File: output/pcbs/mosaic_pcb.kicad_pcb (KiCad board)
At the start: 2 copper layers, 100 x 95 mm, 20 parts

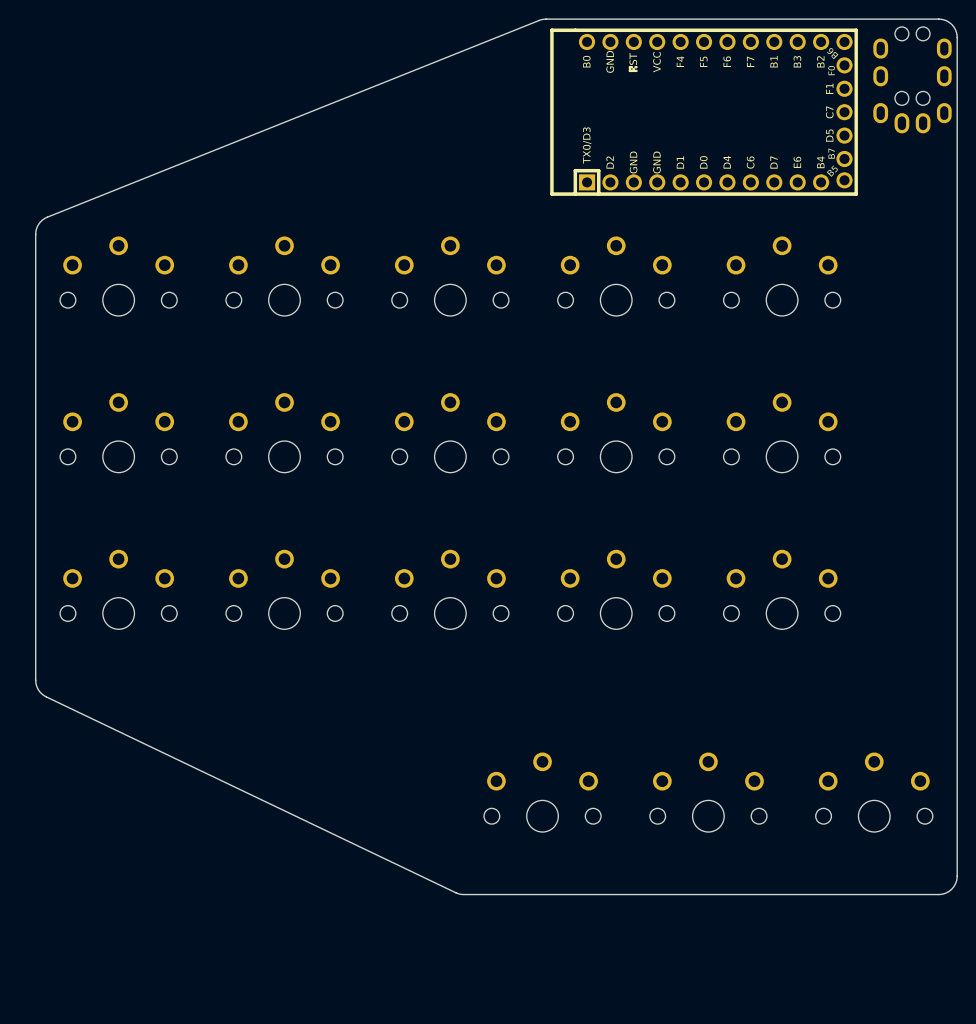
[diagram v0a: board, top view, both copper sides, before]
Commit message: xiao-based, sub 100mm^2
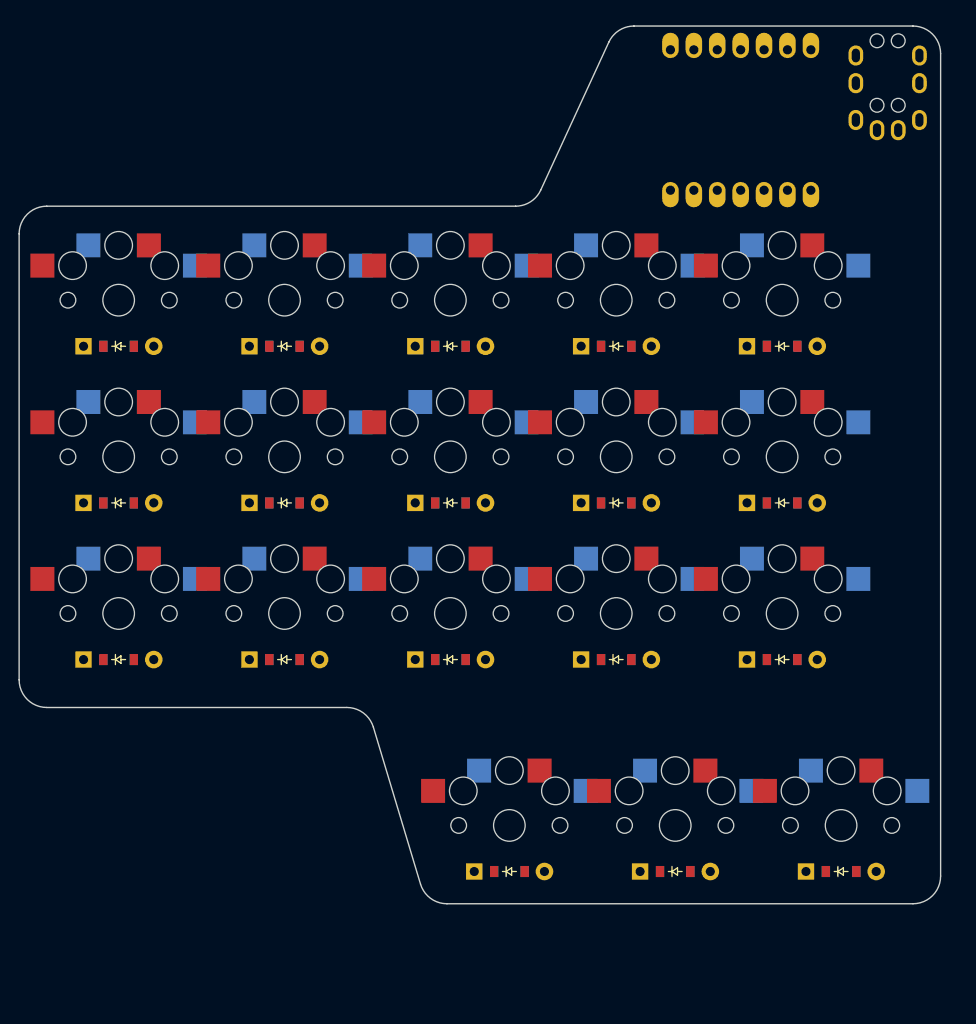
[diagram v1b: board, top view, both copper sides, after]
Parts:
- removed the ? at (208.8, 81.6)
- added ?: , xiao-tht, F.Cu at (211.5, 82.5)
- added D1: , ComboDiode, F.Cu at (144.0, 141.0)
- added D10: , ComboDiode, F.Cu at (198.0, 141.0)
- added D11: , ComboDiode, F.Cu at (198.0, 124.0)
- added D12: , ComboDiode, F.Cu at (198.0, 107.0)
- added D13: , ComboDiode, F.Cu at (216.0, 141.0)
- added D14: , ComboDiode, F.Cu at (216.0, 124.0)
- added D15: , ComboDiode, F.Cu at (216.0, 107.0)
- added D16: , ComboDiode, F.Cu at (186.4, 164.0)
- added D17: , ComboDiode, F.Cu at (204.4, 164.0)
- added D18: , ComboDiode, F.Cu at (222.4, 164.0)
- added D2: , ComboDiode, F.Cu at (144.0, 124.0)
- added D3: , ComboDiode, F.Cu at (144.0, 107.0)
- added D4: , ComboDiode, F.Cu at (162.0, 141.0)
- added D5: , ComboDiode, F.Cu at (162.0, 124.0)
- added D6: , ComboDiode, F.Cu at (162.0, 107.0)
- added D7: , ComboDiode, F.Cu at (180.0, 141.0)
- added D8: , ComboDiode, F.Cu at (180.0, 124.0)
- added D9: , ComboDiode, F.Cu at (180.0, 107.0)
- moved S16 3.74 mm to (186.4, 159.0)
- moved S17 3.74 mm to (204.4, 159.0)
- moved S18 3.74 mm to (222.4, 159.0)
- moved TRRS1 2.80 mm to (228.6, 72.2)
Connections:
- S1 pad 1: matrix_pinky_bottom -> D0
- S1 pad 2: GND -> pinky_bottom
- S10 pad 1: matrix_index_bottom -> D3
- S10 pad 2: GND -> index_bottom
- S11 pad 1: matrix_index_home -> D3
- S11 pad 2: GND -> index_home
- S12 pad 1: matrix_index_top -> D3
- S12 pad 2: GND -> index_top
- S13 pad 1: matrix_inner_bottom -> D4
- S13 pad 2: GND -> inner_bottom
- S14 pad 1: matrix_inner_home -> D4
- S14 pad 2: GND -> inner_home
- S15 pad 1: matrix_inner_top -> D4
- S15 pad 2: GND -> inner_top
- S16 pad 1: thumbfan_near_home -> D2
- S16 pad 2: GND -> near_home
- S17 pad 1: thumbfan_home_home -> D3
- S17 pad 2: GND -> home_home
- S18 pad 1: thumbfan_far_home -> D4
- S18 pad 2: GND -> far_home
- S2 pad 1: matrix_pinky_home -> D0
- S2 pad 2: GND -> pinky_home
- S3 pad 1: matrix_pinky_top -> D0
- S3 pad 2: GND -> pinky_top
- S4 pad 1: matrix_ring_bottom -> D1
- S4 pad 2: GND -> ring_bottom
- S5 pad 1: matrix_ring_home -> D1
- S5 pad 2: GND -> ring_home
- S6 pad 1: matrix_ring_top -> D1
- S6 pad 2: GND -> ring_top
- S7 pad 1: matrix_middle_bottom -> D2
- S7 pad 2: GND -> middle_bottom
- S8 pad 1: matrix_middle_home -> D2
- S8 pad 2: GND -> middle_home
- S9 pad 1: matrix_middle_top -> D2
- S9 pad 2: GND -> middle_top
- TRRS1 pad 2: VCC -> SV
- TRRS1 pad 3: D3 -> D7
- TRRS1 pad 4: D2 -> D6
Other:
- board size 100 x 95 mm -> 100 x 95.2 mm

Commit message: rp2040 zero,diodeless, hotswap
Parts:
- removed the ? at (211.5, 82.5)
- removed D1, D10, D11, D12, D13, D14, D15, D16, D17, D18, D2, D3, D4, D5, D6, D7, D8, D9: , ComboDiode
- added ?: , rp2040_zero_tht_pads, F.Cu at (145.8, 154.7)
- added REF**: VIA-0.6mm, VIA-0.6mm, F.Cu at (144.0, 133.0)
- added REF**: VIA-0.6mm, VIA-0.6mm, F.Cu at (198.0, 133.0)
- added REF**: VIA-0.6mm, VIA-0.6mm, F.Cu at (198.0, 116.0)
- added REF**: VIA-0.6mm, VIA-0.6mm, F.Cu at (198.0, 99.0)
- added REF**: VIA-0.6mm, VIA-0.6mm, F.Cu at (216.0, 133.0)
- added REF**: VIA-0.6mm, VIA-0.6mm, F.Cu at (216.0, 116.0)
- added REF**: VIA-0.6mm, VIA-0.6mm, F.Cu at (216.0, 99.0)
- added REF**: VIA-0.6mm, VIA-0.6mm, F.Cu at (186.4, 160.2)
- added REF**: VIA-0.6mm, VIA-0.6mm, F.Cu at (204.4, 160.2)
- added REF**: VIA-0.6mm, VIA-0.6mm, F.Cu at (222.4, 160.2)
- added REF**: VIA-0.6mm, VIA-0.6mm, F.Cu at (144.0, 116.0)
- added REF**: VIA-0.6mm, VIA-0.6mm, F.Cu at (144.0, 99.0)
- added REF**: VIA-0.6mm, VIA-0.6mm, F.Cu at (162.0, 133.0)
- added REF**: VIA-0.6mm, VIA-0.6mm, F.Cu at (162.0, 116.0)
- added REF**: VIA-0.6mm, VIA-0.6mm, F.Cu at (162.0, 99.0)
- added REF**: VIA-0.6mm, VIA-0.6mm, F.Cu at (180.0, 133.0)
- added REF**: VIA-0.6mm, VIA-0.6mm, F.Cu at (180.0, 116.0)
- added REF**: VIA-0.6mm, VIA-0.6mm, F.Cu at (180.0, 99.0)
- moved TRRS1 78.3 mm to (233.1, 150.4), turned to 270 degrees
- moved S16 4.20 mm to (186.4, 163.2)
- moved S17 4.20 mm to (204.4, 163.2)
- moved S18 4.20 mm to (222.4, 163.2)
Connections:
- S1 pad 1: D0 -> matrix_pinky_bottom
- S1 pad 2: pinky_bottom -> GND
- S10 pad 1: D3 -> matrix_index_bottom
- S10 pad 2: index_bottom -> GND
- S11 pad 1: D3 -> matrix_index_home
- S11 pad 2: index_home -> GND
- S12 pad 1: D3 -> matrix_index_top
- S12 pad 2: index_top -> GND
- S13 pad 1: D4 -> matrix_inner_bottom
- S13 pad 2: inner_bottom -> GND
- S14 pad 1: D4 -> matrix_inner_home
- S14 pad 2: inner_home -> GND
- S15 pad 1: D4 -> matrix_inner_top
- S15 pad 2: inner_top -> GND
- S16 pad 1: D2 -> thumbfan_near_home
- S16 pad 2: near_home -> GND
- S17 pad 1: D3 -> thumbfan_home_home
- S17 pad 2: home_home -> GND
- S18 pad 1: D4 -> thumbfan_far_home
- S18 pad 2: far_home -> GND
- S2 pad 1: D0 -> matrix_pinky_home
- S2 pad 2: pinky_home -> GND
- S3 pad 1: D0 -> matrix_pinky_top
- S3 pad 2: pinky_top -> GND
- S4 pad 1: D1 -> matrix_ring_bottom
- S4 pad 2: ring_bottom -> GND
- S5 pad 1: D1 -> matrix_ring_home
- S5 pad 2: ring_home -> GND
- S6 pad 1: D1 -> matrix_ring_top
- S6 pad 2: ring_top -> GND
- S7 pad 1: D2 -> matrix_middle_bottom
- S7 pad 2: middle_bottom -> GND
- S8 pad 1: D2 -> matrix_middle_home
- S8 pad 2: middle_home -> GND
- S9 pad 1: D2 -> matrix_middle_top
- S9 pad 2: middle_top -> GND
- TRRS1 pad 1: GND -> 3V3
- TRRS1 pad 2: SV -> GND
- TRRS1 pad 3: D7 -> GP9
- TRRS1 pad 4: D6 -> GP8
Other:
- board size 100 x 95.2 mm -> 100 x 81.6 mm

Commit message: routing tweaks
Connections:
- ? pad 1: matrix_pinky_bottom -> matrix_pinky_top
- ? pad 11: matrix_middle_top -> matrix_middle_bottom
- ? pad 12: matrix_inner_bottom -> matrix_inner_top
- ? pad 14: matrix_inner_top -> matrix_inner_bottom
- ? pad 3: matrix_pinky_top -> matrix_pinky_bottom
- ? pad 7: matrix_middle_bottom -> matrix_middle_top
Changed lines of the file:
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@@
       (at 145.8 154.7 90)
       (attr through_hole)
-      (pad 1 thru_hole oval (at 7.62 -10.16 270) (size 2.5 1.5) (drill 1 (offset -0.5 0)) (layers *.Cu *.Mask) (net 1 "matrix_pinky_bottom"))
+      (pad 1 thru_hole oval (at 7.62 -10.16 270) (size 2.5 1.5) (drill 1 (offset -0.5 0)) (layers *.Cu *.Mask) (net 4 "matrix_pinky_top"))
       (pad 2 thru_hole oval (at 7.62 -7.62 270) (size 2.5 1.5) (drill 1 (offset -0.5 0)) (layers *.Cu *.Mask) (net 3 "matrix_pinky_home"))
-      (pad 3 thru_hole oval (at 7.62 -5.08 270) (size 2.5 1.5) (drill 1 (offset -0.5 0)) (layers *.Cu *.Mask) (net 4 "matrix_pinky_top"))
+      (pad 3 thru_hole oval (at 7.62 -5.08 270) (size 2.5 1.5) (drill 1 (offset -0.5 0)) (layers *.Cu *.Mask) (net 1 "matrix_pinky_bottom"))
       (pad 4 thru_hole oval (at 7.62 -2.54 270) (size 2.5 1.5) (drill 1 (offset -0.5 0)) (layers *.Cu *.Mask) (net 7 "matrix_ring_top"))
       (pad 5 thru_hole oval (at 7.62 0 270) (size 2.5 1.5) (drill 1 (offset -0.5 0)) (layers *.Cu *.Mask) (net 6 "matrix_ring_home"))
       (pad 6 thru_hole oval (at 7.62 2.54 270) (size 2.5 1.5) (drill 1 (offset -0.5 0)) (layers *.Cu *.Mask) (net 5 "matrix_ring_bottom"))
-      (pad 7 thru_hole oval (at 7.62 5.08 270) (size 2.5 1.5) (drill 1 (offset -0.5 0)) (layers *.Cu *.Mask) (net 8 "matrix_middle_bottom"))
+      (pad 7 thru_hole oval (at 7.62 5.08 270) (size 2.5 1.5) (drill 1 (offset -0.5 0)) (layers *.Cu *.Mask) (net 10 "matrix_middle_top"))
       (pad 8 thru_hole oval (at 7.62 7.62 270) (size 2.5 1.5) (drill 1 (offset -0.5 0)) (layers *.Cu *.Mask) (net 9 "matrix_middle_home"))
       (pad 9 thru_hole oval (at 7.62 10.16 270) (size 2.5 1.5) (drill 1 (offset -0.5 0)) (layers *.Cu *.Mask) (net 20 "GP8"))
       (pad 10 thru_hole oval (at 5.08 10.16 180) (size 2.5 1.5) (drill 1 (offset -0.5 0)) (layers *.Cu *.Mask) (net 21 "GP9"))
-      (pad 11 thru_hole oval (at 2.54 10.16 180) (size 2.5 1.5) (drill 1 (offset -0.5 0)) (layers *.Cu *.Mask) (net 10 "matrix_middle_top"))
-      (pad 12 thru_hole oval (at 0 10.16 180) (size 2.5 1.5) (drill 1 (offset -0.5 0)) (layers *.Cu *.Mask) (net 14 "matrix_inner_bottom"))
+      (pad 11 thru_hole oval (at 2.54 10.16 180) (size 2.5 1.5) (drill 1 (offset -0.5 0)) (layers *.Cu *.Mask) (net 8 "matrix_middle_bottom"))
+      (pad 12 thru_hole oval (at 0 10.16 180) (size 2.5 1.5) (drill 1 (offset -0.5 0)) (layers *.Cu *.Mask) (net 16 "matrix_inner_top"))
       (pad 13 thru_hole oval (at -2.54 10.16 180) (size 2.5 1.5) (drill 1 (offset -0.5 0)) (layers *.Cu *.Mask) (net 15 "matrix_inner_home"))
-      (pad 14 thru_hole oval (at -5.08 10.16 180) (size 2.5 1.5) (drill 1 (offset -0.5 0)) (layers *.Cu *.Mask) (net 16 "matrix_inner_top"))
+      (pad 14 thru_hole oval (at -5.08 10.16 180) (size 2.5 1.5) (drill 1 (offset -0.5 0)) (layers *.Cu *.Mask) (net 14 "matrix_inner_bottom"))
       (pad 15 thru_hole oval (at -7.62 10.16 90) (size 2.5 1.5) (drill 1 (offset -0.5 0)) (layers *.Cu *.Mask) (net 13 "matrix_index_top"))
       (pad 16 thru_hole oval (at -7.62 7.62 90) (size 2.5 1.5) (drill 1 (offset -0.5 0)) (layers *.Cu *.Mask) (net 12 "matrix_index_home"))

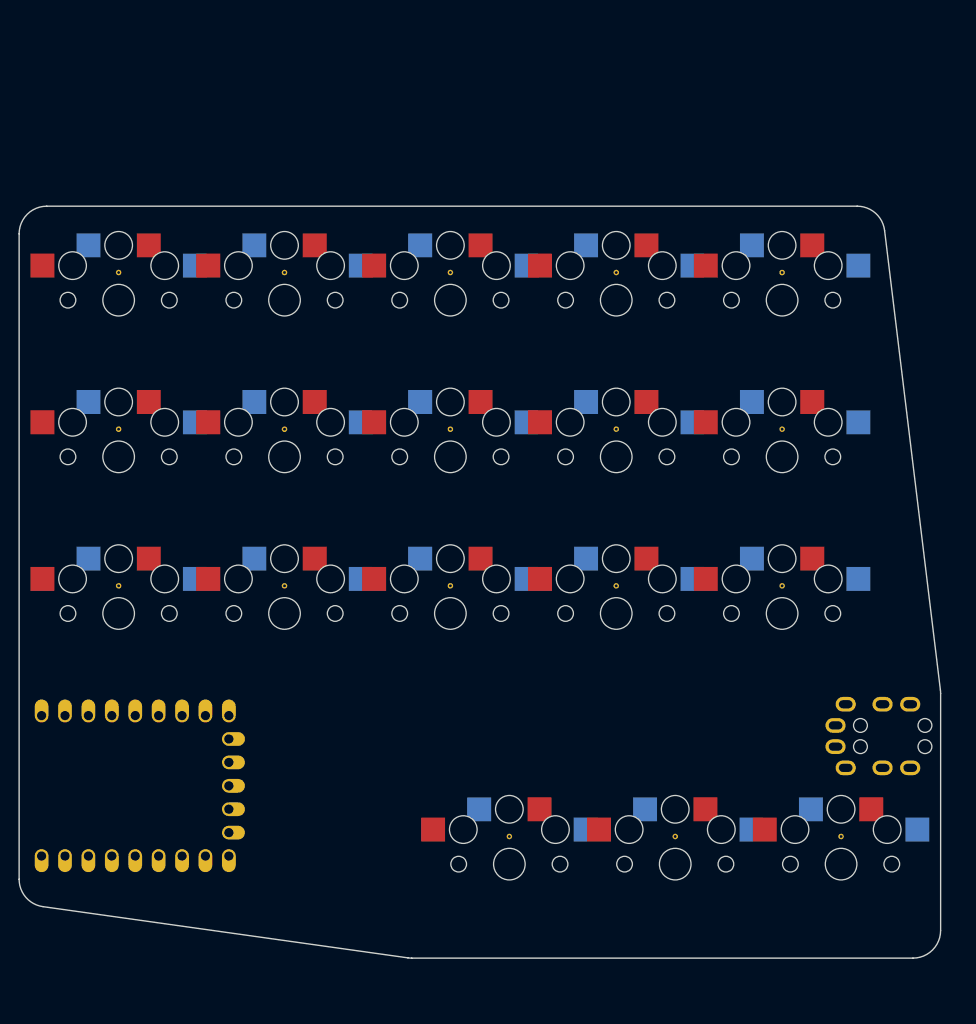
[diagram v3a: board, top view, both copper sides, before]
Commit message: remove hotswap
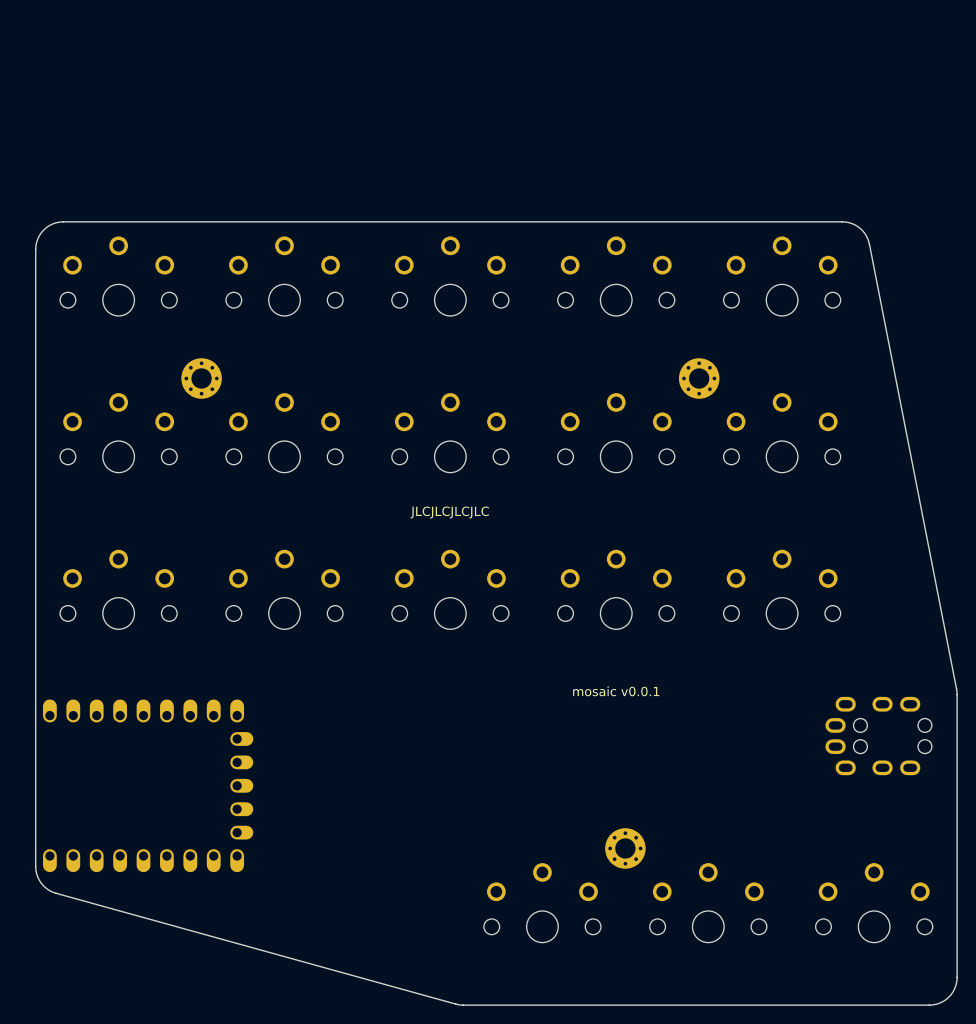
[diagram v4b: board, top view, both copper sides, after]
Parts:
- removed REF** (x18): VIA-0.6mm, VIA-0.6mm
- added _2: , MountingHole_2.2mm_M2_Pad_Via, F.Cu at (153.0, 110.5)
- added _3: , MountingHole_2.2mm_M2_Pad_Via, F.Cu at (199.0, 161.5)
- added _4: , MountingHole_2.2mm_M2_Pad_Via, F.Cu at (207.0, 110.5)
- moved S16 7.69 mm to (190.0, 170.0)
- moved S17 7.69 mm to (208.0, 170.0)
- moved S18 7.69 mm to (226.0, 170.0)
- moved ? 0.90 mm to (146.7, 154.7)
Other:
- board size 100 x 81.6 mm -> 100 x 85 mm
- board text added: "JLCJLCJLCJLC"
- board text added: "mosaic v0.0.1"
